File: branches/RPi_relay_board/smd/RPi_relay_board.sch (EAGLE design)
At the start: 48 parts, among them IC1 LM340S-05, K1 351, K2 351, T1 ZXTN2020F, T2 ZXTN2020F, T3 ZXTN2020F, U1 MAX232SOIC16

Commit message: Version 2.0-series of pcb
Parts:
- removed C10: 100nF, rcl:C-EUC2012
- removed C11: 10uF, rcl:C-EUC3216
- removed C12: 330nF, SparkFun:CAP_POL7343
- removed IC1: LM340S-05, LM1084IS:LM340S-05
- C4: value 330nF -> 100nF; device rcl:C-EUC3216 -> rcl:C-EUC2012
- C5: device rcl:C-EUC3216 -> rcl:C-EUC2012
- C9: value 100nF -> 330nF; device rcl:C-EUC2012 -> SparkFun:CAP_POL7343
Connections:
- net +12V: no longer C4.1, IC1.VI
- net +5V: no longer C3.1, IC1.VO
- net 3.3V: now also C3.1, C4.2, C6.1; no longer C5.1, C6.2, C8.1
- net GND: now also C6.2, C9.-; no longer C11.2, C12.-, C4.2, C7.2, C8.2, IC1.GND
- net N$10: now also C9.+; no longer C11.1, C12.+
- net N$13: now also C7.2; no longer C9.2
- net N$31: now also C8.2; no longer C10.2
- net N$32: now also C7.1; no longer C9.1
- net N$35: now also C8.1; no longer C10.1
- net N$36: now also C4.1; no longer C6.1
- net N$37: now also C5.1; no longer C7.1
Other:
- moved on the sheet: C2, C3, C4, C5, C6, C7, C8

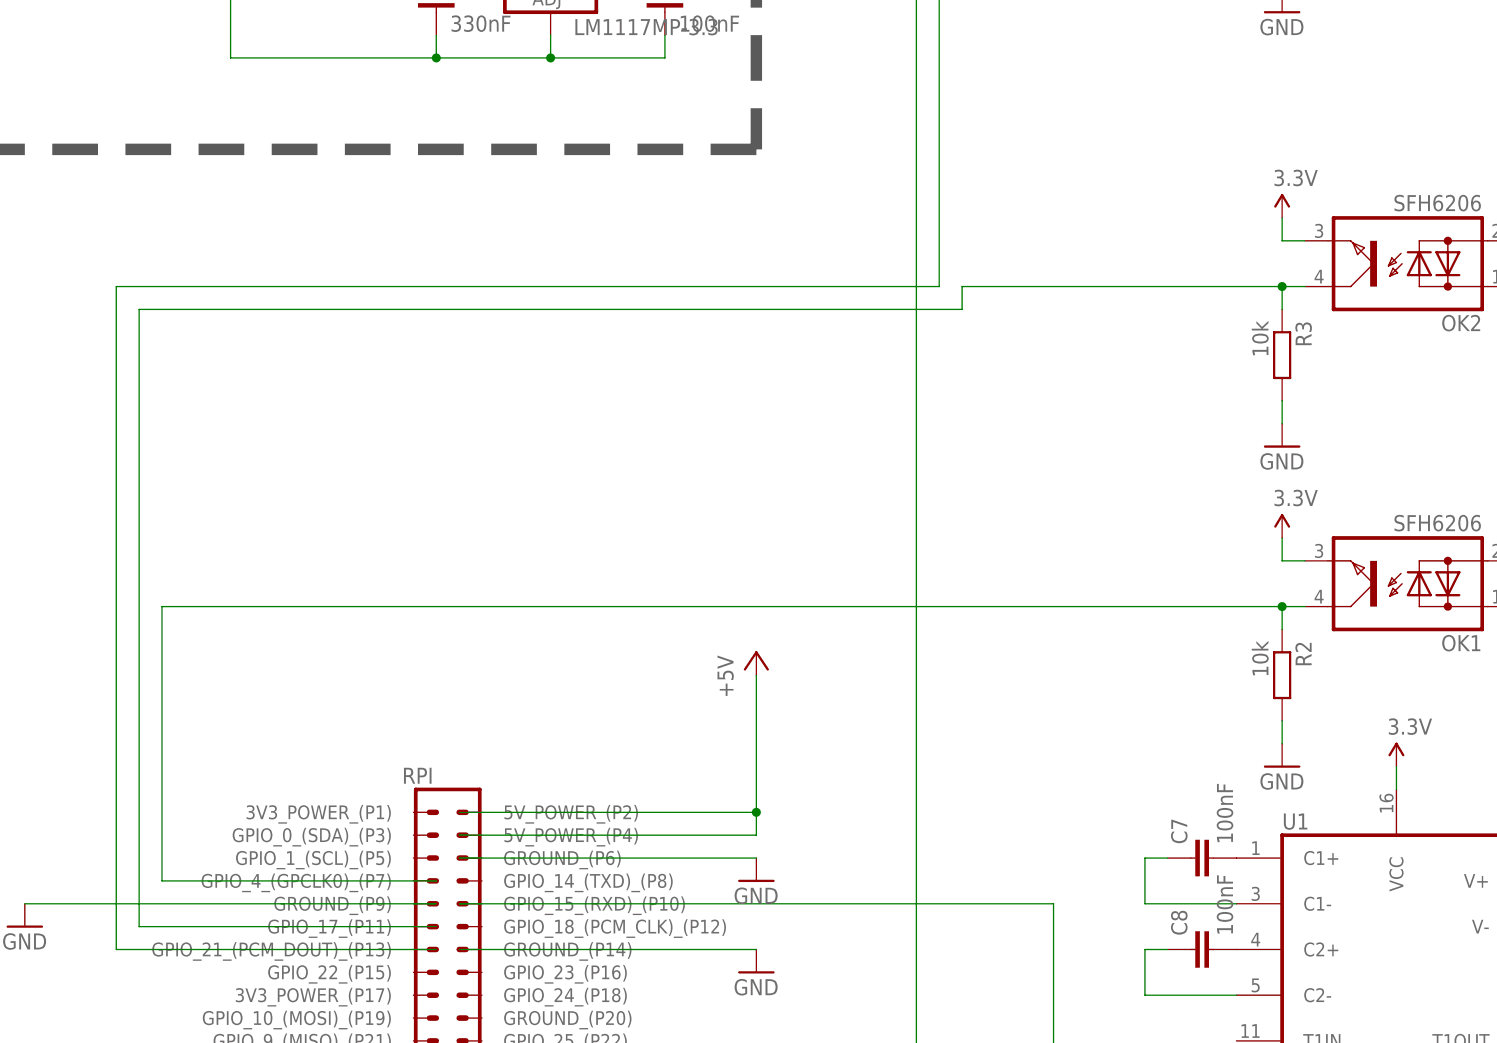
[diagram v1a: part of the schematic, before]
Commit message: input opto's was wrong polarity on output
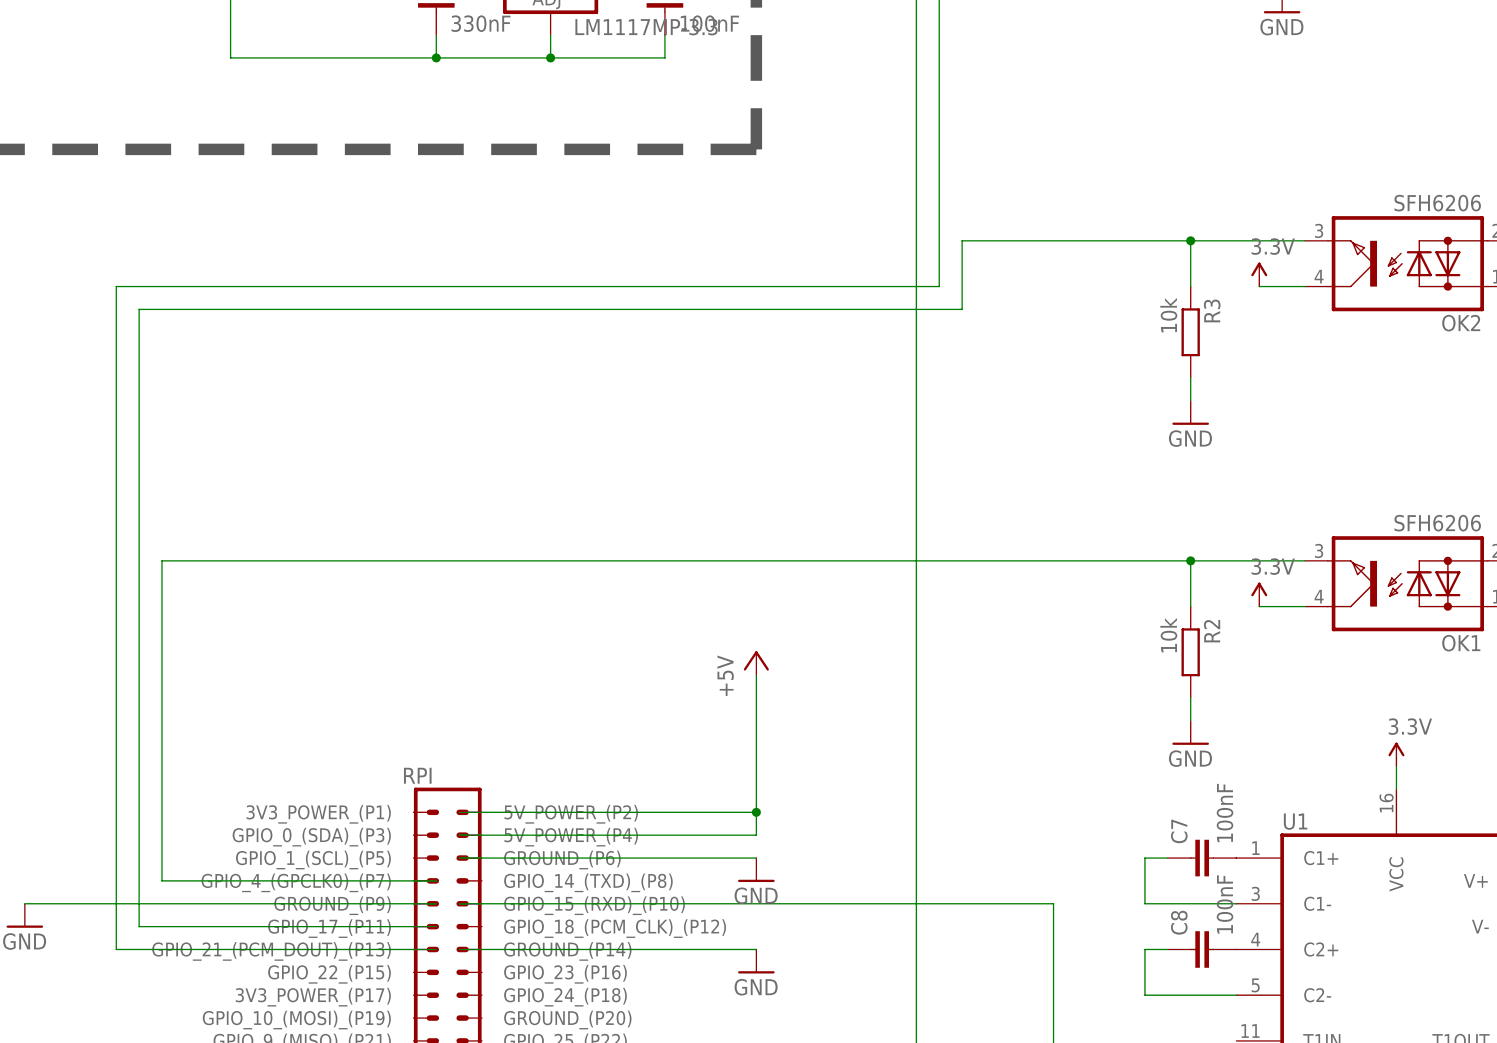
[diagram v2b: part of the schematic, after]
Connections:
- net 3.3V: now also OK1.C, OK2.C; no longer OK1.E, OK2.E
- net N$1: now also OK2.E; no longer OK2.C
- net N$4: now also OK1.E; no longer OK1.C
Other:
- moved on the sheet: R2, R3
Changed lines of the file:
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@@
 <instance part="GND" gate="1" x="58.42" y="86.36"/>
 <instance part="GND11" gate="1" x="152.4" y="71.12"/>
-<instance part="GND10" gate="1" x="152.4" y="22.86"/>
+<instance part="GND10" gate="1" x="142.24" y="25.4"/>
 <instance part="24V" gate="1" x="58.42" y="124.46"/>
 <instance part="R5" gate="G$1" x="187.96" y="45.72" rot="R180"/>
@@
 <instance part="K1" gate="2" x="276.86" y="15.24"/>
 <instance part="K1" gate="3" x="276.86" y="0"/>
-<instance part="R3" gate="G$1" x="152.4" y="33.02" rot="R270"/>
-<instance part="GND2" gate="1" x="152.4" y="-12.7"/>
+<instance part="R3" gate="G$1" x="142.24" y="35.56" rot="R270"/>
+<instance part="GND2" gate="1" x="142.24" y="-10.16"/>
 <instance part="R4" gate="G$1" x="187.96" y="10.16" rot="R180"/>
-<instance part="R2" gate="G$1" x="152.4" y="-2.54" rot="R270"/>
+<instance part="R2" gate="G$1" x="142.24" y="0" rot="R270"/>
 <instance part="GND3" gate="1" x="180.34" y="-2.54"/>
 <instance part="GND5" gate="1" x="180.34" y="33.02"/>
@@
 <instance part="24V5" gate="1" x="170.18" y="190.5"/>
 <instance part="GND19" gate="1" x="170.18" y="152.4"/>
-<instance part="P+2" gate="G$1" x="152.4" y="12.7"/>
-<instance part="P+3" gate="G$1" x="152.4" y="48.26"/>
+<instance part="P+2" gate="G$1" x="149.86" y="5.08"/>
+<instance part="P+3" gate="G$1" x="149.86" y="40.64"/>
 <instance part="P+4" gate="G$1" x="205.74" y="55.88"/>
 <instance part="P+5" gate="G$1" x="205.74" y="20.32"/>
@@
 <pinref part="R3" gate="G$1" pin="2"/>
 <pinref part="GND10" gate="1" pin="GND"/>
-<wire x1="152.4" y1="27.94" x2="152.4" y2="25.4" width="0.1524" layer="91"/>
+<wire x1="142.24" y1="30.48" x2="142.24" y2="27.94" width="0.1524" layer="91"/>
 </segment>
 <segment>
 <pinref part="R2" gate="G$1" pin="2"/>
 <pinref part="GND2" gate="1" pin="GND"/>
-<wire x1="152.4" y1="-7.62" x2="152.4" y2="-10.16" width="0.1524" layer="91"/>
+<wire x1="142.24" y1="-5.08" x2="142.24" y2="-7.62" width="0.1524" layer="91"/>
 </segment>
 <segment>
@@
 <net name="N$1" class="0">
 <segment>
-<pinref part="R3" gate="G$1" pin="1"/>
-<wire x1="152.4" y1="40.64" x2="152.4" y2="38.1" width="0.1524" layer="91"/>
-<wire x1="116.84" y1="40.64" x2="152.4" y2="40.64" width="0.1524" layer="91"/>
-<wire x1="116.84" y1="40.64" x2="116.84" y2="38.1" width="0.1524" layer="91"/>
 <wire x1="116.84" y1="38.1" x2="25.4" y2="38.1" width="0.1524" layer="91"/>
 <wire x1="25.4" y1="38.1" x2="25.4" y2="-30.48" width="0.1524" layer="91"/>
 <pinref part="RPI" gate="A" pin="GPIO_17_(P11)"/>
 <wire x1="25.4" y1="-30.48" x2="58.42" y2="-30.48" width="0.1524" layer="91"/>
-<pinref part="OK2" gate="G$1" pin="C"/>
-<wire x1="152.4" y1="40.64" x2="154.94" y2="40.64" width="0.1524" layer="91"/>
-<junction x="152.4" y="40.64"/>
+<wire x1="116.84" y1="38.1" x2="116.84" y2="45.72" width="0.1524" layer="91"/>
+<pinref part="OK2" gate="G$1" pin="E"/>
+<wire x1="116.84" y1="45.72" x2="142.24" y2="45.72" width="0.1524" layer="91"/>
+<pinref part="R3" gate="G$1" pin="1"/>
+<wire x1="142.24" y1="45.72" x2="154.94" y2="45.72" width="0.1524" layer="91"/>
+<wire x1="142.24" y1="40.64" x2="142.24" y2="45.72" width="0.1524" layer="91"/>
+<junction x="142.24" y="45.72"/>
 </segment>
 </net>
@@
 <segment>
 <pinref part="R2" gate="G$1" pin="1"/>
-<wire x1="152.4" y1="5.08" x2="152.4" y2="2.54" width="0.1524" layer="91"/>
-<wire x1="152.4" y1="5.08" x2="27.94" y2="5.08" width="0.1524" layer="91"/>
-<wire x1="27.94" y1="5.08" x2="27.94" y2="-25.4" width="0.1524" layer="91"/>
+<wire x1="142.24" y1="10.16" x2="142.24" y2="5.08" width="0.1524" layer="91"/>
+<wire x1="142.24" y1="10.16" x2="27.94" y2="10.16" width="0.1524" layer="91"/>
+<wire x1="27.94" y1="10.16" x2="27.94" y2="-25.4" width="0.1524" layer="91"/>
 <pinref part="RPI" gate="A" pin="GPIO_4_(GPCLK0)_(P7)"/>
 <wire x1="27.94" y1="-25.4" x2="58.42" y2="-25.4" width="0.1524" layer="91"/>
-<pinref part="OK1" gate="G$1" pin="C"/>
-<wire x1="152.4" y1="5.08" x2="154.94" y2="5.08" width="0.1524" layer="91"/>
-<junction x="152.4" y="5.08"/>
+<pinref part="OK1" gate="G$1" pin="E"/>
+<wire x1="154.94" y1="10.16" x2="142.24" y2="10.16" width="0.1524" layer="91"/>
+<junction x="142.24" y="10.16"/>
 </segment>
 </net>
@@
 </segment>
 <segment>
-<wire x1="152.4" y1="10.16" x2="152.4" y2="12.7" width="0.1524" layer="91"/>
-<pinref part="P+2" gate="G$1" pin="3.3V"/>
-<pinref part="OK1" gate="G$1" pin="E"/>
-<wire x1="154.94" y1="10.16" x2="152.4" y2="10.16" width="0.1524" layer="91"/>
-</segment>
-<segment>
-<wire x1="152.4" y1="45.72" x2="152.4" y2="48.26" width="0.1524" layer="91"/>
-<pinref part="P+3" gate="G$1" pin="3.3V"/>
-<pinref part="OK2" gate="G$1" pin="E"/>
-<wire x1="152.4" y1="45.72" x2="154.94" y2="45.72" width="0.1524" layer="91"/>
-</segment>
-<segment>
 <wire x1="205.74" y1="48.26" x2="205.74" y2="55.88" width="0.1524" layer="91"/>
 <pinref part="P+4" gate="G$1" pin="3.3V"/>
@@
 <wire x1="165.1" y1="-12.7" x2="165.1" y2="-15.24" width="0.1524" layer="91"/>
 </segment>
-</net>
+<segment>
+<pinref part="P+3" gate="G$1" pin="3.3V"/>
+<pinref part="OK2" gate="G$1" pin="C"/>
+<wire x1="149.86" y1="40.64" x2="154.94" y2="40.64" width="0.1524" layer="91"/>
+</segment>
+<segment>
+<pinref part="P+2" gate="G$1" pin="3.3V"/>
+<pinref part="OK1" gate="G$1" pin="C"/>
+<wire x1="149.86" y1="5.08" x2="154.94" y2="5.08" width="0.1524" layer="91"/>
+</segment>
+</net>
